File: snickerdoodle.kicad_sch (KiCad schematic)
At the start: 11 parts, among them J2 TFM-115-01-F-D-A, J3 TFM-120-01-F-D-A, U601 TCA9800

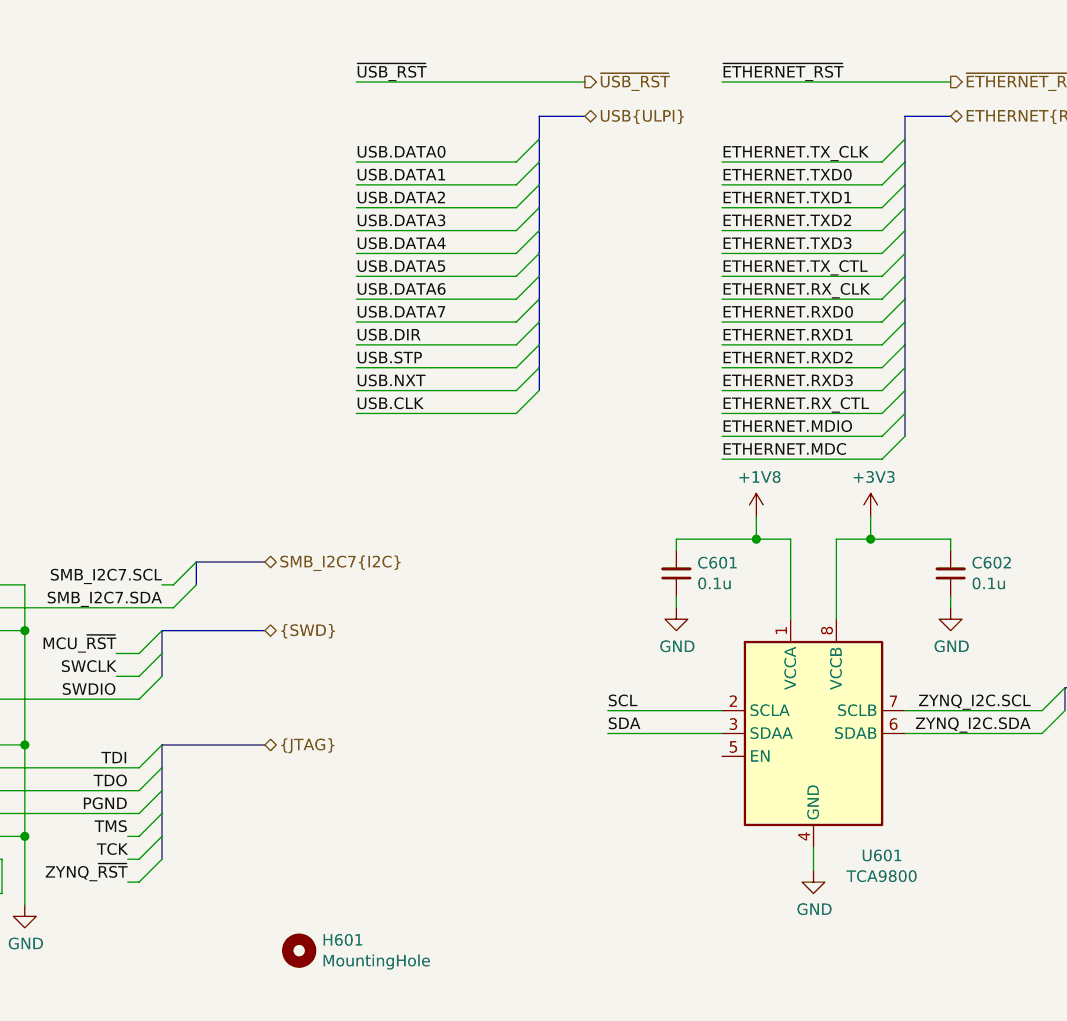
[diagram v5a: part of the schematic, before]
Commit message: Expand PCB, change to inches, center Snickerdoodle
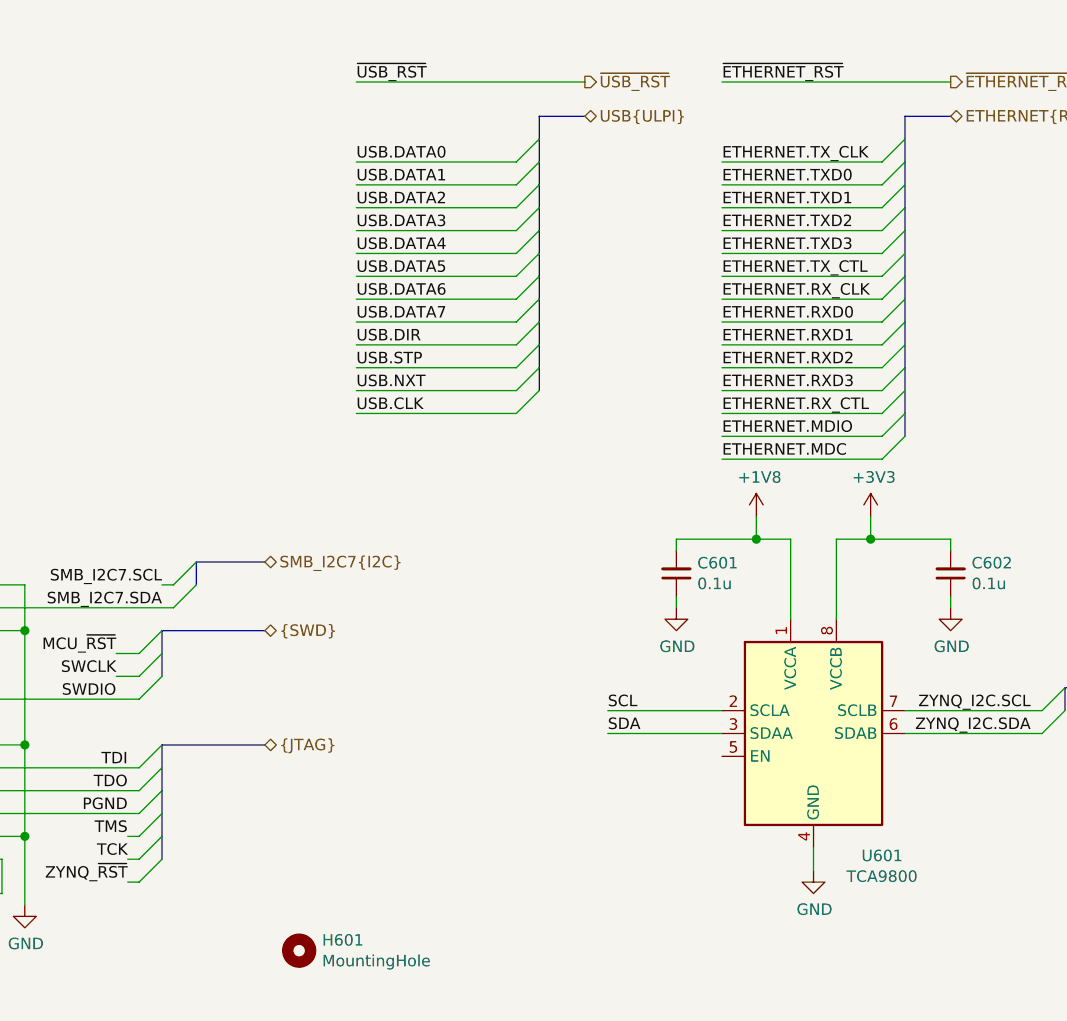
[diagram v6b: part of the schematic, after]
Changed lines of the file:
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@@
-(kicad_sch (version 20200714) (host eeschema "5.99.0-unknown-9b6ade6b1~102~ubuntu20.04.1")
+(kicad_sch (version 20200714) (host eeschema "5.99.0-unknown-829316fad~102~ubuntu20.04.1")
   (page 6 15)
   (paper "B")
@@
     (stroke (width 0) (type solid) (color 0 0 0 0))
   )
-  (bus (pts (xy 287.02 191.77) (xy 287.02 194.31))
+  (bus (pts (xy 287.02 191.77) (xy 287.02 196.85))
     (stroke (width 0) (type solid) (color 0 0 0 0))
   )
@@
     (stroke (width 0) (type solid) (color 0 0 0 0))
   )
-  (bus (pts (xy 287.02 194.31) (xy 287.02 199.39))
-    (stroke (width 0) (type solid) (color 0 0 0 0))
-  )
-  (bus (pts (xy 287.02 199.39) (xy 287.02 204.47))
+  (bus (pts (xy 287.02 196.85) (xy 287.02 201.93))
+    (stroke (width 0) (type solid) (color 0 0 0 0))
+  )
+  (bus (pts (xy 287.02 201.93) (xy 287.02 204.47))
     (stroke (width 0) (type solid) (color 0 0 0 0))
   )
@@
     (stroke (width 0) (type solid) (color 0 0 0 0))
   )
-  (bus (pts (xy 328.93 127) (xy 328.93 132.08))
-    (stroke (width 0) (type solid) (color 0 0 0 0))
-  )
-  (bus (pts (xy 328.93 132.08) (xy 328.93 137.16))
-    (stroke (width 0) (type solid) (color 0 0 0 0))
-  )
-  (bus (pts (xy 328.93 137.16) (xy 328.93 142.24))
-    (stroke (width 0) (type solid) (color 0 0 0 0))
-  )
-  (bus (pts (xy 328.93 142.24) (xy 328.93 144.78))
+  (bus (pts (xy 328.93 127) (xy 328.93 129.54))
+    (stroke (width 0) (type solid) (color 0 0 0 0))
+  )
+  (bus (pts (xy 328.93 129.54) (xy 328.93 134.62))
+    (stroke (width 0) (type solid) (color 0 0 0 0))
+  )
+  (bus (pts (xy 328.93 134.62) (xy 328.93 139.7))
+    (stroke (width 0) (type solid) (color 0 0 0 0))
+  )
+  (bus (pts (xy 328.93 139.7) (xy 328.93 144.78))
     (stroke (width 0) (type solid) (color 0 0 0 0))
   )
@@
     (stroke (width 0) (type solid) (color 0 0 0 0))
   )
-  (bus (pts (xy 369.57 127) (xy 369.57 129.54))
-    (stroke (width 0) (type solid) (color 0 0 0 0))
-  )
-  (bus (pts (xy 369.57 129.54) (xy 369.57 134.62))
+  (bus (pts (xy 369.57 127) (xy 369.57 132.08))
+    (stroke (width 0) (type solid) (color 0 0 0 0))
+  )
+  (bus (pts (xy 369.57 132.08) (xy 369.57 134.62))
     (stroke (width 0) (type solid) (color 0 0 0 0))
   )
@@
     (stroke (width 0) (type solid) (color 0 0 0 0))
   )
-  (bus (pts (xy 369.57 139.7) (xy 369.57 142.24))
-    (stroke (width 0) (type solid) (color 0 0 0 0))
-  )
-  (bus (pts (xy 369.57 142.24) (xy 369.57 147.32))
-    (stroke (width 0) (type solid) (color 0 0 0 0))
-  )
-  (bus (pts (xy 369.57 147.32) (xy 369.57 152.4))
-    (stroke (width 0) (type solid) (color 0 0 0 0))
-  )
-  (bus (pts (xy 369.57 152.4) (xy 369.57 157.48))
-    (stroke (width 0) (type solid) (color 0 0 0 0))
-  )
+  (bus (pts (xy 369.57 139.7) (xy 369.57 144.78))
+    (stroke (width 0) (type solid) (color 0 0 0 0))
+  )
+  (bus (pts (xy 369.57 144.78) (xy 369.57 149.86))
+    (stroke (width 0) (type solid) (color 0 0 0 0))
+  )
+  (bus (pts (xy 369.57 149.86) (xy 369.57 154.94))
+    (stroke (width 0) (type solid) (color 0 0 0 0))
+  )
+  (bus (pts (xy 369.57 154.94) (xy 369.57 157.48))
+    (stroke (width 0) (type solid) (color 0 0 0 0))
+  )

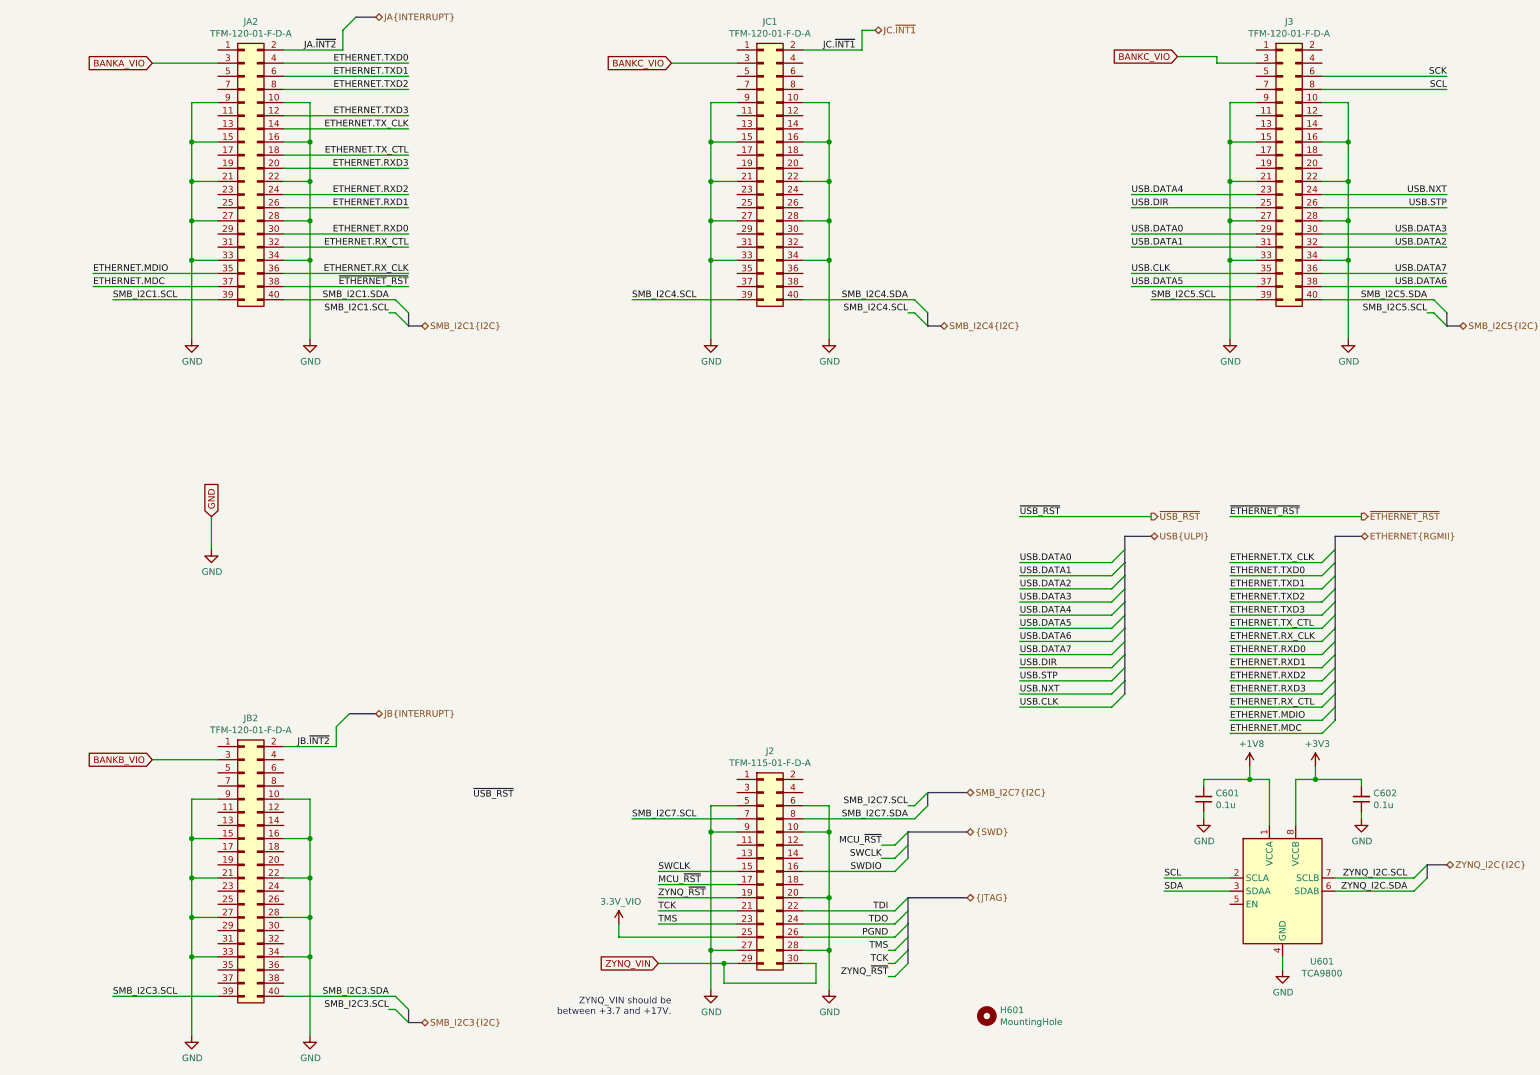
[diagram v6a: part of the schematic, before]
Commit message: Move Ethernet PHY to left side of board
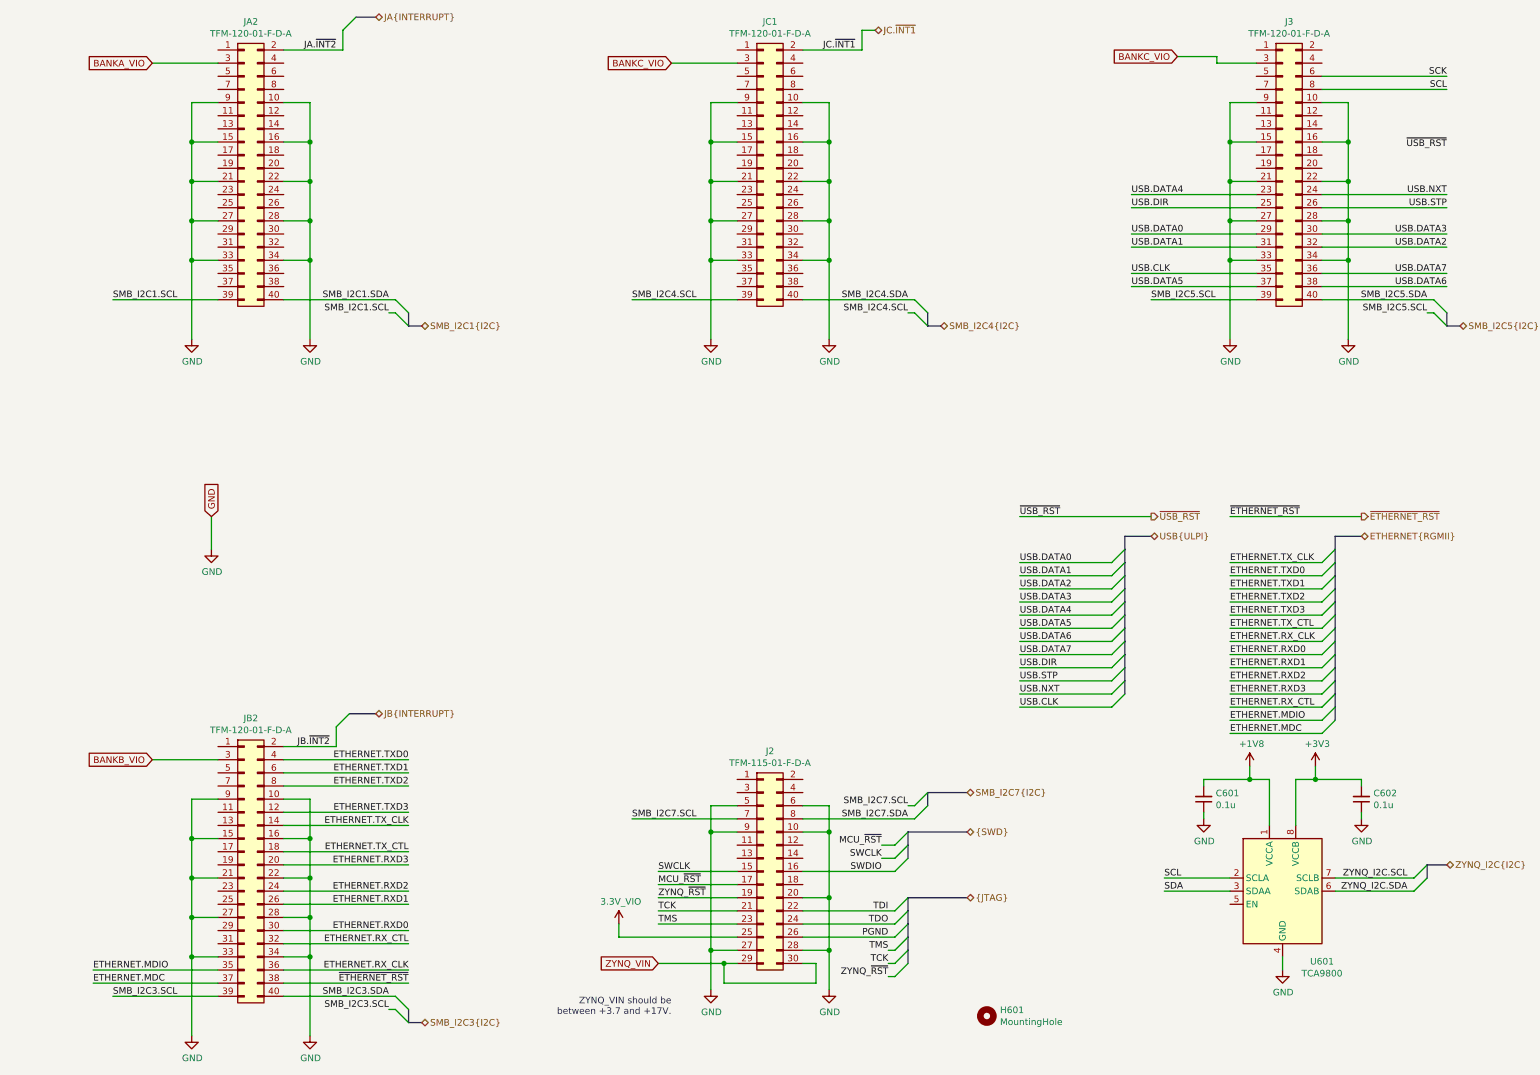
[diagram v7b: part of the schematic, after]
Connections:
- net ETHERNET.MDC: now also JB2.37 (Pin_37); no longer JA2.37 (Pin_37)
- net ETHERNET.MDIO: now also JB2.35 (Pin_35); no longer JA2.35 (Pin_35)
- net ETHERNET.RXD0: now also JB2.30 (Pin_30); no longer JA2.30 (Pin_30)
- net ETHERNET.RXD1: now also JB2.26 (Pin_26); no longer JA2.26 (Pin_26)
- net ETHERNET.RXD2: now also JB2.24 (Pin_24); no longer JA2.24 (Pin_24)
- net ETHERNET.RXD3: now also JB2.20 (Pin_20); no longer JA2.20 (Pin_20)
- net ETHERNET.RX_CLK: now also JB2.36 (Pin_36); no longer JA2.36 (Pin_36)
- net ETHERNET.RX_CTL: now also JB2.32 (Pin_32); no longer JA2.32 (Pin_32)
- net ETHERNET.TXD0: now also JB2.4 (Pin_4); no longer JA2.4 (Pin_4)
- net ETHERNET.TXD1: now also JB2.6 (Pin_6); no longer JA2.6 (Pin_6)
- net ETHERNET.TXD2: now also JB2.8 (Pin_8); no longer JA2.8 (Pin_8)
- net ETHERNET.TXD3: now also JB2.12 (Pin_12); no longer JA2.12 (Pin_12)
- net ETHERNET.TX_CLK: now also JB2.14 (Pin_14); no longer JA2.14 (Pin_14)
- net ETHERNET.TX_CTL: now also JB2.18 (Pin_18); no longer JA2.18 (Pin_18)
- net ~ETHERNET_RST: now also JB2.38 (Pin_38); no longer JA2.38 (Pin_38)
